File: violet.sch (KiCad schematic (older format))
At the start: 16 parts, among them J1 NEIGHBOR1, J2 NEIGHBOR2, J7 BONUS_ROW, U1 M24C02-FMN6TP

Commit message: set up initial configuration of headers
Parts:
- removed C1: 100nF, Capacitor_SMD:C_0603_1608Metric_Pad1.05x0.95mm_HandSolder, symbol Device:C
- removed JP1, JP2, JP3: Jumper_3_Bridged12, neighbor:0603-JUMPER-3-BRIDGED12, symbol Jumper:Jumper_3_Bridged12
- removed R1: 10k, Resistor_SMD:R_0603_1608Metric_Pad1.05x0.95mm_HandSolder, symbol Device:R
- removed U1: M24C02-FMN6TP, Package_SO:SOIC-8_3.9x4.9mm_P1.27mm, symbol Memory_EEPROM:M24C02-FMN
- added C?: C, symbol Device:C
- added U?: 74HC4051, symbol 74xx:74HC4051
- added U? (x2): PCA9698, symbol gsg-symbols:PCA9698
- J1, J2, J? (x2): Description CONN RCPT .100\" 40POS DUAL-ROW STACKING GOLD -> CONN HEADER VERT 20POS 2.54MM; Manufacturer Samtec -> Adam Tech; Note Alternate: SSQ-120-x3-x-D -> (none); Part Number SSQ-120-23-G-D -> PH2-20-UA
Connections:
- net labels added: EUT_VCC
- net labels removed: E0, E1, E2
- wire segments 231 -> 220
- no-connect marks 20 -> 122
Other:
- note added: "EUT"
- note added: "Gladiolus testing unit should have the IR LEDS soldered on to the\nopposite side of the board from Gladiolus."
- note added: "Plug Gladiolus testing unit in here."
- note removed: "J7 is optional"
- note removed: "Pins with no-connect flags may affect Azalea (mainboard)\nboot. Do not use them unless you study Azalea to\nunderstand the consequences."
- note removed: "WC is by default pulled up, enabling write protection.\nTo disable write protection temporarily, configure P2_1\n(J2_P35) as GPIO and output low. To disable write\nprotection permanently, remove R1."
- note removed: "board-to-board connections"
- note removed: "neighbor identification EEPROM (optional)"

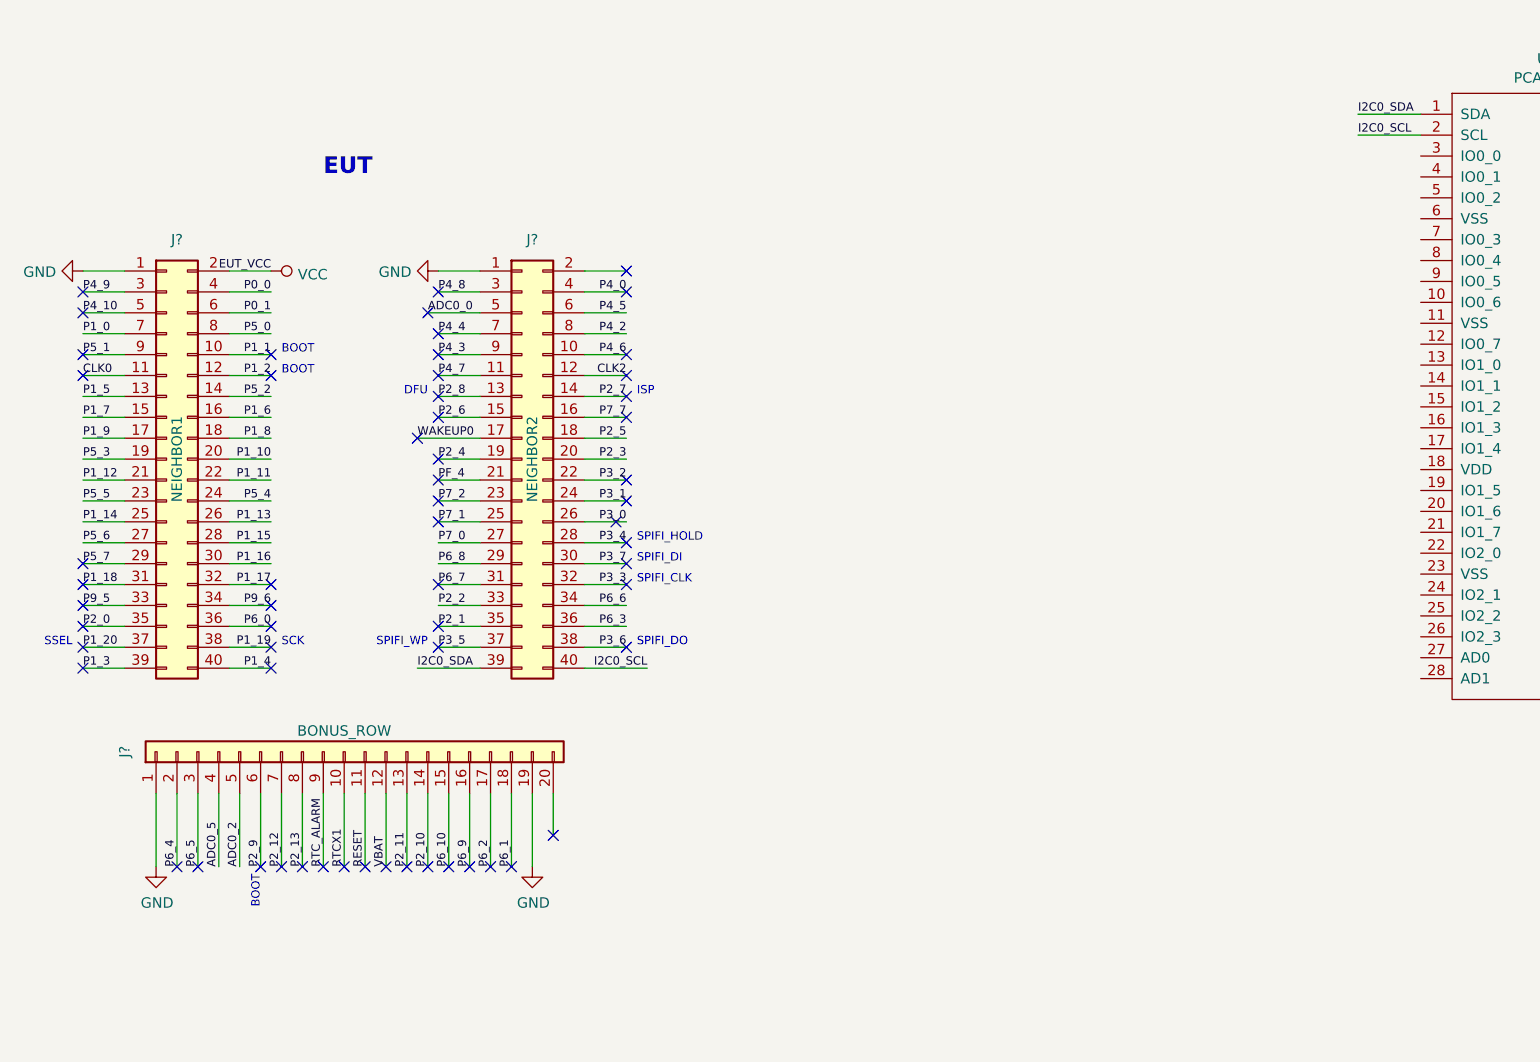
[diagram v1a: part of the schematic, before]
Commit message: Add header set for EUT Azalea; wire RX/TX signals between EUT and EUT Azalea
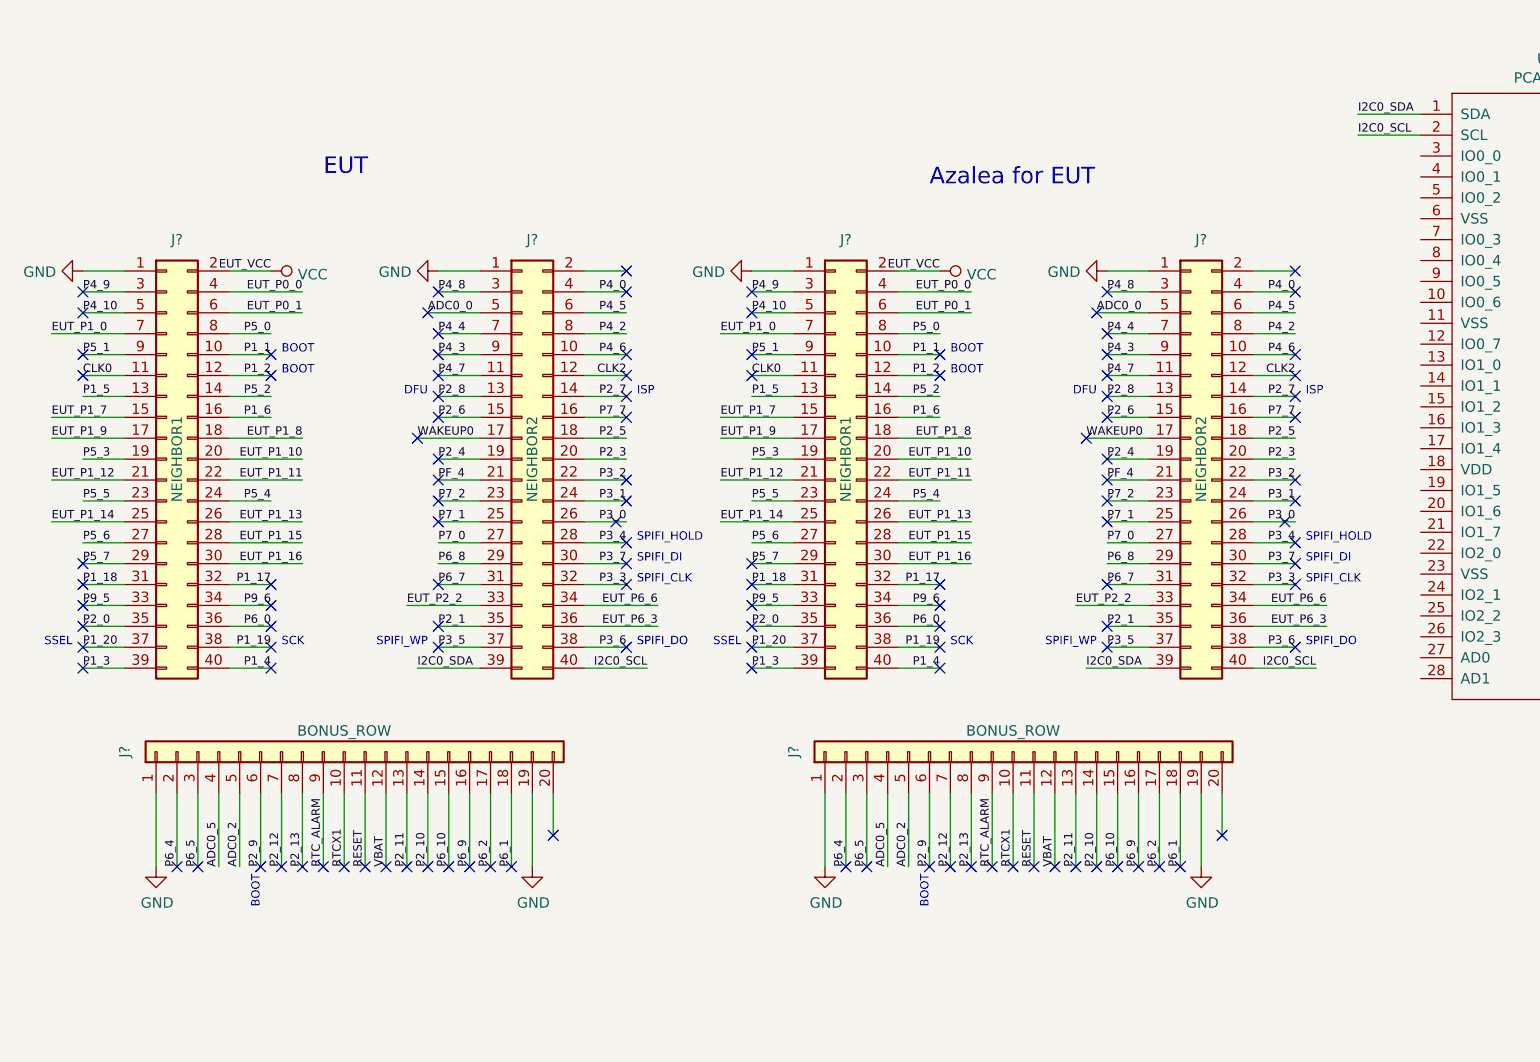
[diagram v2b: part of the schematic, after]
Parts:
- added J?: NEIGHBOR2, neighbor:HEADER-2x20, symbol Connector_Generic:Conn_02x20_Odd_Even
- added J?: NEIGHBOR1, neighbor:HEADER-2x20, symbol Connector_Generic:Conn_02x20_Odd_Even
- added J?: BONUS_ROW, neighbor:HEADER-1x20, symbol Connector_Generic:Conn_01x20
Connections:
- net ADC0_0: now also J?.5 (Pin_5)
- net ADC0_2: now also J?.5 (Pin_5)
- net ADC0_5: now also J?.4 (Pin_4)
- net CLK0: now also J?.11 (Pin_11)
- net CLK2: now also J?.12 (Pin_12)
- net GND: now also J?.1 (Pin_1), J?.1 (Pin_1), J?.1 (Pin_1), J?.19 (Pin_19)
- net I2C0_SCL: now also J?.40 (Pin_40)
- net I2C0_SDA: now also J?.39 (Pin_39)
- net P0_0: no longer J?.4 (Pin_4)
- net P0_1: no longer J?.6 (Pin_6)
- net P1_0: no longer J?.7 (Pin_7)
- net P1_1: now also J?.10 (Pin_10)
- net P1_10: no longer J?.20 (Pin_20)
- net P1_11: no longer J?.22 (Pin_22)
- net P1_12: no longer J?.21 (Pin_21)
- net P1_13: no longer J?.26 (Pin_26)
- net P1_14: no longer J?.25 (Pin_25)
- net P1_15: no longer J?.28 (Pin_28)
- net P1_16: no longer J?.30 (Pin_30)
- net P1_17: now also J?.32 (Pin_32)
- net P1_18: now also J?.31 (Pin_31)
- net P1_19: now also J?.38 (Pin_38)
- net P1_2: now also J?.12 (Pin_12)
- net P1_20: now also J?.37 (Pin_37)
- net P1_3: now also J?.39 (Pin_39)
- net P1_4: now also J?.40 (Pin_40)
- net P1_5: now also J?.13 (Pin_13)
- net P1_6: now also J?.16 (Pin_16)
- net P1_7: no longer J?.15 (Pin_15)
- net P1_8: no longer J?.18 (Pin_18)
- net P1_9: no longer J?.17 (Pin_17)
- net P2_0: now also J?.35 (Pin_35)
- net P2_1: now also J?.35 (Pin_35)
- net P2_10: now also J?.14 (Pin_14)
- net P2_11: now also J?.13 (Pin_13)
- net P2_12: now also J?.7 (Pin_7)
- net P2_13: now also J?.8 (Pin_8)
- net P2_2: no longer J?.33 (Pin_33)
- net P2_3: now also J?.20 (Pin_20)
- net P2_4: now also J?.19 (Pin_19)
- net P2_5: now also J?.18 (Pin_18)
- net P2_6: now also J?.15 (Pin_15)
- net P2_7: now also J?.14 (Pin_14)
- net P2_8: now also J?.13 (Pin_13)
- net P2_9: now also J?.6 (Pin_6)
- net P3_0: now also J?.26 (Pin_26)
- net P3_1: now also J?.24 (Pin_24)
- net P3_2: now also J?.22 (Pin_22)
- net P3_3: now also J?.32 (Pin_32)
- net P3_4: now also J?.28 (Pin_28)
- net P3_5: now also J?.37 (Pin_37)
- net P3_6: now also J?.38 (Pin_38)
- net P3_7: now also J?.30 (Pin_30)
- net P4_0: now also J?.4 (Pin_4)
- net P4_10: now also J?.5 (Pin_5)
- net P4_2: now also J?.8 (Pin_8)
- net P4_3: now also J?.9 (Pin_9)
- net P4_4: now also J?.7 (Pin_7)
- net P4_5: now also J?.6 (Pin_6)
- net P4_6: now also J?.10 (Pin_10)
- net P4_7: now also J?.11 (Pin_11)
- net P4_8: now also J?.3 (Pin_3)
- net P4_9: now also J?.3 (Pin_3)
- net P5_0: now also J?.8 (Pin_8)
- net P5_1: now also J?.9 (Pin_9)
- net P5_2: now also J?.14 (Pin_14)
- net P5_3: now also J?.19 (Pin_19)
- net P5_4: now also J?.24 (Pin_24)
- net P5_5: now also J?.23 (Pin_23)
- net P5_6: now also J?.27 (Pin_27)
- net P5_7: now also J?.29 (Pin_29)
- net P6_0: now also J?.36 (Pin_36)
- net P6_1: now also J?.18 (Pin_18)
- net P6_10: now also J?.15 (Pin_15)
- net P6_2: now also J?.17 (Pin_17)
- net P6_3: no longer J?.36 (Pin_36)
- net P6_4: now also J?.2 (Pin_2)
- net P6_5: now also J?.3 (Pin_3)
- net P6_6: no longer J?.34 (Pin_34)
- net P6_7: now also J?.31 (Pin_31)
- net P6_8: now also J?.29 (Pin_29)
- net P6_9: now also J?.16 (Pin_16)
- net P7_0: now also J?.27 (Pin_27)
- net P7_1: now also J?.25 (Pin_25)
- net P7_2: now also J?.23 (Pin_23)
- net P7_7: now also J?.16 (Pin_16)
- net P9_5: now also J?.33 (Pin_33)
- net P9_6: now also J?.34 (Pin_34)
- net PF_4: now also J?.21 (Pin_21)
- net RESET: now also J?.11 (Pin_11)
- net RTCX1: now also J?.10 (Pin_10)
- net RTC_ALARM: now also J?.9 (Pin_9)
- net VBAT: now also J?.12 (Pin_12)
- net VCC: now also J?.2 (Pin_2)
- net WAKEUP0: now also J?.17 (Pin_17)
- new net EUT_P0_0: J?.4 (Pin_4), J?.4 (Pin_4)
- new net EUT_P0_1: J?.6 (Pin_6), J?.6 (Pin_6)
- new net EUT_P1_0: J?.7 (Pin_7), J?.7 (Pin_7)
- new net EUT_P1_10: J?.20 (Pin_20), J?.20 (Pin_20)
- new net EUT_P1_11: J?.22 (Pin_22), J?.22 (Pin_22)
- new net EUT_P1_12: J?.21 (Pin_21), J?.21 (Pin_21)
- new net EUT_P1_13: J?.26 (Pin_26), J?.26 (Pin_26)
- new net EUT_P1_14: J?.25 (Pin_25), J?.25 (Pin_25)
- new net EUT_P1_15: J?.28 (Pin_28), J?.28 (Pin_28)
- new net EUT_P1_16: J?.30 (Pin_30), J?.30 (Pin_30)
- new net EUT_P1_7: J?.15 (Pin_15), J?.15 (Pin_15)
- new net EUT_P1_8: J?.18 (Pin_18), J?.18 (Pin_18)
- new net EUT_P1_9: J?.17 (Pin_17), J?.17 (Pin_17)
- new net EUT_P2_2: J?.33 (Pin_33), J?.33 (Pin_33)
- new net EUT_P6_3: J?.36 (Pin_36), J?.36 (Pin_36)
- new net EUT_P6_6: J?.34 (Pin_34), J?.34 (Pin_34)
- no-connect marks 122 -> 183
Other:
- note added: "Azalea for EUT"

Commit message: Add labels to I/O expanders and headers
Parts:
- added C? (x2): C, symbol Device:C
- added R? (x7): R, symbol Device:R
- added U?: AP2553W6-7, symbol gsg-symbols:NX5P2553GV
- C?: value C -> 100nF; footprint (none) -> gsg-modules:0603; Description (none) -> CAP CER 0.1UF 16V 20% X7R 0603; Manufacturer (none) -> Kemet; Part Number (none) -> C0603C104M4RAC
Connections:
- net +5V: now also C?.1, U?.1 (VIN)
- net ADC0_0: no longer J?.5 (Pin_5)
- net CLK0: no longer J?.11 (Pin_11)
- net CLK2: no longer J?.12 (Pin_12)
- net EUT_P1_10: no longer J?.20 (Pin_20)
- net EUT_P1_11: no longer J?.22 (Pin_22)
- net EUT_P1_12: no longer J?.21 (Pin_21)
- net EUT_P1_13: no longer J?.26 (Pin_26)
- net EUT_P1_14: no longer J?.25 (Pin_25)
- net EUT_P1_7: no longer J?.15 (Pin_15)
- net EUT_P1_8: no longer J?.18 (Pin_18)
- net EUT_P1_9: no longer J?.17 (Pin_17)
- net GND: now also U?.11 (VSS), U?.11 (VSS), U?.23 (VSS), U?.23 (VSS), U?.27 (AD0), U?.34 (VSS), U?.34 (VSS), U?.39 (VSS), U?.39 (VSS), U?.51 (VSS), U?.51 (VSS), U?.6 (VSS), U?.6 (VSS), C?.2, C?.2, R?.2, R?.2, U?.2 (GND); no longer J?.1 (Pin_1), J?.1 (Pin_1), J?.19 (Pin_19)
- net I2C0_SCL: no longer J?.40 (Pin_40)
- net I2C0_SDA: no longer J?.39 (Pin_39)
- net P1_1: no longer J?.10 (Pin_10)
- net P1_13: now also U?.55 (~INT~), R?.2
- net P1_16: now also U?.56 (~RESET~), R?.2
- net P1_17: no longer J?.32 (Pin_32)
- net P1_18: no longer J?.31 (Pin_31)
- net P1_19: no longer J?.38 (Pin_38)
- net P1_2: no longer J?.12 (Pin_12)
- net P1_20: no longer J?.37 (Pin_37)
- net P1_3: no longer J?.39 (Pin_39)
- net P1_4: no longer J?.40 (Pin_40)
- net P1_5: no longer J?.13 (Pin_13)
- net P1_6: no longer J?.16 (Pin_16)
- net P2_0: no longer J?.35 (Pin_35)
- net P2_1: no longer J?.35 (Pin_35)
- net P2_10: no longer J?.14 (Pin_14)
- net P2_11: no longer J?.13 (Pin_13)
- net P2_12: no longer J?.7 (Pin_7)
- net P2_13: no longer J?.8 (Pin_8)
- net P2_3: no longer J?.20 (Pin_20)
- net P2_4: no longer J?.19 (Pin_19)
- net P2_5: no longer J?.18 (Pin_18)
- net P2_6: no longer J?.15 (Pin_15)
- net P2_7: no longer J?.14 (Pin_14)
- net P2_8: no longer J?.13 (Pin_13)
- net P2_9: no longer J?.6 (Pin_6)
- net P3_0: no longer J?.26 (Pin_26)
- net P3_1: no longer J?.24 (Pin_24)
- net P3_2: no longer J?.22 (Pin_22)
- net P3_3: no longer J?.32 (Pin_32)
- net P3_4: no longer J?.28 (Pin_28)
- net P3_5: no longer J?.37 (Pin_37)
- net P3_6: no longer J?.38 (Pin_38)
- net P3_7: no longer J?.30 (Pin_30)
- net P4_0: now also U?.10 (S1); no longer J?.4 (Pin_4)
- net P4_10: no longer J?.5 (Pin_5)
- net P4_2: now also R?.1, U?.3 (EN); no longer J?.8 (Pin_8)
- net P4_3: no longer J?.9 (Pin_9)
- net P4_4: now also U?.11 (S0); no longer J?.7 (Pin_7)
- net P4_5: now also U?.6 (~E); no longer J?.6 (Pin_6), J?.6 (Pin_6)
- net P4_6: now also R?.2, U?.4 (FAULT); no longer J?.10 (Pin_10)
- net P4_7: no longer J?.11 (Pin_11)
- net P4_8: now also U?.9 (S2); no longer J?.3 (Pin_3)
- net P4_9: no longer J?.3 (Pin_3)
- net P5_0: no longer J?.8 (Pin_8)
- net P5_1: no longer J?.9 (Pin_9)
- net P5_2: no longer J?.14 (Pin_14)
- net P5_3: no longer J?.19 (Pin_19)
- net P5_4: no longer J?.24 (Pin_24)
- net P5_5: no longer J?.23 (Pin_23)
- net P5_6: no longer J?.27 (Pin_27)
- net P5_7: no longer J?.29 (Pin_29)
- net P6_0: no longer J?.36 (Pin_36)
- net P6_1: no longer J?.18 (Pin_18)
- net P6_10: no longer J?.15 (Pin_15)
- net P6_2: no longer J?.17 (Pin_17)
- net P6_4: no longer J?.2 (Pin_2)
- net P6_5: no longer J?.3 (Pin_3)
- net P6_7: no longer J?.31 (Pin_31)
- net P6_8: no longer J?.29 (Pin_29)
- net P6_9: no longer J?.16 (Pin_16)
- net P7_0: no longer J?.27 (Pin_27)
- net P7_1: no longer J?.25 (Pin_25)
- net P7_2: no longer J?.23 (Pin_23)
- net P7_7: no longer J?.16 (Pin_16)
- net P9_5: now also U?.55 (~INT~), R?.2; no longer J?.33 (Pin_33)
- net P9_6: now also U?.56 (~RESET~), R?.2; no longer J?.34 (Pin_34)
- net PF_4: no longer J?.21 (Pin_21)
- net RESET: no longer J?.11 (Pin_11)
- net RTCX1: no longer J?.10 (Pin_10)
- net RTC_ALARM: no longer J?.9 (Pin_9)
- net VBAT: no longer J?.12 (Pin_12)
- net VCC: now also U?.18 (VDD), U?.18 (VDD), U?.27 (AD0), U?.28 (AD1), U?.28 (AD1), U?.29 (AD2), U?.29 (AD2), U?.46 (VDD), U?.46 (VDD), R?.1, R?.1, R?.1, R?.1, R?.1
- net WAKEUP0: no longer J?.17 (Pin_17)
- net U2IO0_5: now reaches J?.20 (Pin_20)
- net U2IO0_5: now also U?.9 (IO0_5)
- net U1IO1_3: now reaches U?.16 (IO1_3)
- net U1IO1_3: now also J?.35 (Pin_35)
- net U1IO1_4: now reaches U?.17 (IO1_4)
- net U1IO1_4: now also J?.34 (Pin_34)
- net U1IO1_5: now reaches U?.19 (IO1_5)
- net U1IO1_5: now also J?.33 (Pin_33)
- net U1IO1_6: now reaches U?.20 (IO1_6)
- net U1IO1_6: now also J?.32 (Pin_32)
- net U1IO1_7: now reaches U?.21 (IO1_7)
- net U1IO1_7: now also J?.31 (Pin_31)
- net U1IO2_0: now reaches U?.22 (IO2_0)
- net U1IO2_1: now reaches U?.24 (IO2_1)
- net U1IO2_1: now also J?.29 (Pin_29)
- net U1IO2_2: now reaches U?.25 (IO2_2)
- net U1IO2_3: now reaches U?.26 (IO2_3)
- net U1IO2_3: now also J?.27 (Pin_27)
- net U1IO0_0: now reaches U?.3 (IO0_0)
- net U1IO0_0: now also J?.2 (Pin_2)
- net U1IO2_4: now reaches U?.31 (IO2_4)
- net U1IO2_4: now also J?.26 (Pin_26)
- net U1IO2_5: now reaches U?.32 (IO2_5)
- net U1IO2_5: now also J?.25 (Pin_25)
- net U1IO2_6: now reaches U?.33 (IO2_6)
- net U1IO2_6: now also J?.24 (Pin_24)
- net U1IO2_7: now reaches U?.35 (IO2_7)
- net U1IO2_7: now also J?.23 (Pin_23)
- net U1IO3_0: now reaches U?.36 (IO3_0)
- net U1IO3_0: now also J?.22 (Pin_22), U?.36 (IO3_0)
- net U1IO3_1: now reaches U?.37 (IO3_1)
- net U1IO3_1: now also J?.21 (Pin_21)
- net U1IO3_2: now reaches U?.38 (IO3_2)
- net U1IO3_2: now also J?.20 (Pin_20)
- net U1IO0_1: now reaches U?.4 (IO0_1)
- net U1IO0_1: now also J?.1 (Pin_1)
- net U1IO3_3: now reaches U?.40 (IO3_3)
- net U1IO3_3: now also J?.19 (Pin_19)
- net U1IO3_4: now reaches U?.41 (IO3_4)
- net U1IO3_4: now also J?.18 (Pin_18)
- net U1IO3_5: now reaches U?.42 (IO3_5)
- net U1IO3_5: now also J?.17 (Pin_17)
- net U1IO3_6: now reaches U?.43 (IO3_6)
- net U1IO3_6: now also J?.16 (Pin_16)
- net U1IO3_7: now reaches U?.44 (IO3_7)
- net U1IO3_7: now also J?.15 (Pin_15)
- net U1IO4_0: now reaches U?.45 (IO4_0)
- net U1IO4_0: now also J?.14 (Pin_14)
- net U1IO4_1: now reaches U?.47 (IO4_1)
- net U1IO4_1: now also J?.13 (Pin_13)
- net U1IO4_2: now reaches U?.48 (IO4_2)
- net U1IO4_2: now also J?.12 (Pin_12)
- net U1IO4_3: now reaches U?.49 (IO4_3)
- net U1IO4_3: now also J?.10 (Pin_10)
- net U1IO4_4: now reaches U?.50 (IO4_4)
- net U1IO4_4: now also J?.9 (Pin_9)
- net U1IO4_5: now reaches U?.52 (IO4_5)
- net U1IO4_5: now also J?.8 (Pin_8)
- net U1IO4_6: now reaches U?.53 (IO4_6)
- net U1IO4_6: now also J?.5 (Pin_5)
- net U1IO4_7: now reaches U?.54 (IO4_7)
- net U1IO4_7: now also J?.3 (Pin_3)
- net U2IO0_6: now reaches U?.10 (IO0_6)
- net U2IO0_6: now also J?.19 (Pin_19)
- net U2IO0_7: now reaches U?.12 (IO0_7)
- net U2IO0_7: now also J?.18 (Pin_18)
- net U2IO1_0: now reaches U?.13 (IO1_0)
- net U2IO1_0: now also J?.17 (Pin_17)
- net U2IO1_1: now reaches U?.14 (IO1_1)
- net U2IO1_1: now also J?.16 (Pin_16)
- net U2IO1_2: now reaches U?.15 (IO1_2)
- net U2IO1_2: now also J?.15 (Pin_15)
- net U2IO1_3: now reaches U?.16 (IO1_3)
- net U2IO1_3: now also J?.14 (Pin_14)
- net U2IO1_4: now reaches U?.17 (IO1_4)
- net U2IO1_4: now also J?.13 (Pin_13)
- net U2IO1_5: now reaches U?.19 (IO1_5)
- net U2IO1_5: now also J?.12 (Pin_12)
- net U2IO1_6: now reaches U?.20 (IO1_6)
- net U2IO1_6: now also J?.10 (Pin_10)
- net U2IO1_7: now reaches U?.21 (IO1_7)
- net U2IO1_7: now also J?.9 (Pin_9)
- net U2IO2_0: now reaches U?.22 (IO2_0)
- net U2IO2_0: now also J?.8 (Pin_8)
- net U2IO2_1: now reaches U?.24 (IO2_1)
- net U2IO2_1: now also J?.7 (Pin_7)
- net U2IO2_2: now reaches U?.25 (IO2_2)
- net U2IO2_2: now also J?.6 (Pin_6)
- net U2IO2_3: now reaches U?.26 (IO2_3)
- net U2IO2_3: now also J?.3 (Pin_3)
- net U2IO2_4: now reaches U?.31 (IO2_4)
- net U2IO2_4: now also J?.1 (Pin_1)
- net U2IO2_5: now reaches U?.32 (IO2_5)
- net U2IO2_5: now also J?.4 (Pin_4)
- net U2IO2_6: now reaches U?.33 (IO2_6)
- net U2IO2_6: now also J?.3 (Pin_3)
- net U2IO2_7: now reaches U?.35 (IO2_7)
- net U2IO3_1: now reaches U?.37 (IO3_1)
- net U2IO3_1: now also J?.7 (Pin_7)
- net U2IO3_2: now reaches U?.38 (IO3_2)
- net U2IO3_2: now also J?.10 (Pin_10)
- net U2IO3_3: now reaches U?.40 (IO3_3)
- net U2IO3_3: now also J?.9 (Pin_9)
- net U2IO3_5: now reaches U?.42 (IO3_5)
- net U2IO3_5: now also J?.13 (Pin_13)
- net U2IO3_7: now reaches U?.44 (IO3_7)
- net U2IO3_7: now also J?.15 (Pin_15)
- new net: R?.1, U?.5 (ILIM)
- new net EUT_5V: C?.1, U?.6 (VOUT)
- new net EUT_ADCCLK: J?.6 (Pin_6), J?.6 (Pin_6)
- new net U2IO3_0: J?.8 (Pin_8)
- no-connect marks 183 -> 151
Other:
- note added: "No connects are TPs on Narcissus"
- moved on the sheet: J?, U?
